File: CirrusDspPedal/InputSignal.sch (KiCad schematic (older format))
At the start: 12 parts, among them J1 MonoJack2Switch, U1 CS5343, U2 74AHC1G126

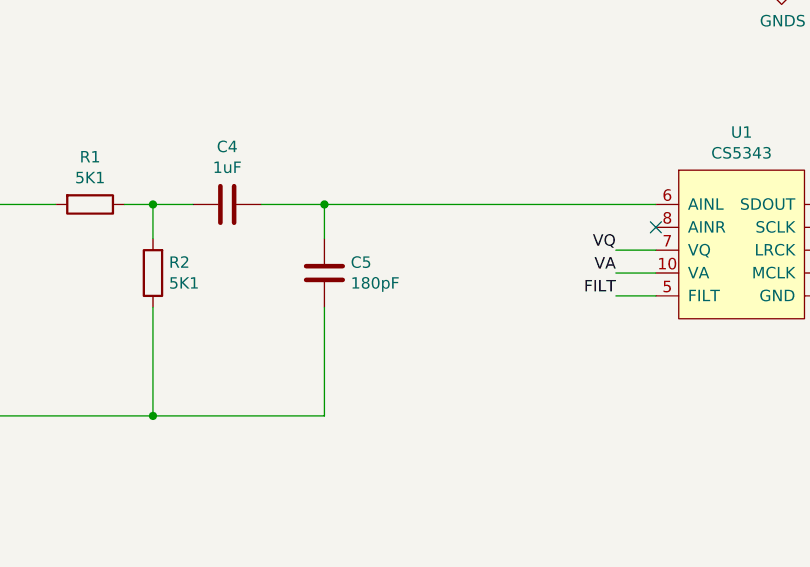
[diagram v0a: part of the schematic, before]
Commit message: Added Footswitches and relay
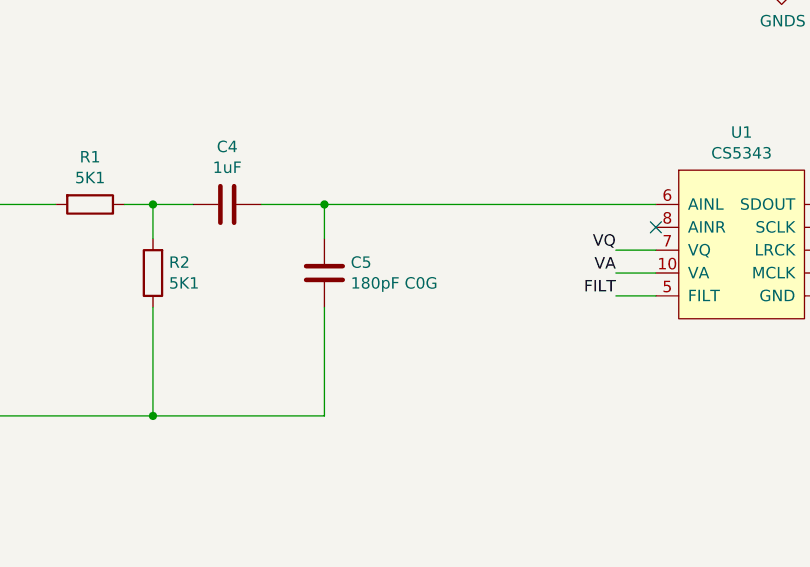
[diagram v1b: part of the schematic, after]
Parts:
- C5: value 180pF -> 180pF C0G
- J1: footprint (none) -> NeutrikNRJ:NRJxHx_NOTAB
- U2: footprint (none) -> Package_TO_SOT_SMD:SOT-23-5_HandSoldering
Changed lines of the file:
@@
 $Descr A4 11693 8268
 encoding utf-8
-Sheet 2 8
+Sheet 2 10
 Title ""
 Date ""
@@
 F 0 "J1" H 2695 4400 50  0000 C CNN
 F 1 "MonoJack2Switch" H 2695 4309 50  0000 C CNN
-F 2 "" H 2600 4075 50  0001 C CNN
+F 2 "NeutrikNRJ:NRJxHx_NOTAB" H 2600 4075 50  0001 C CNN
 F 3 "" H 2600 4075 50  0001 C CNN
 	1    2600 4025
@@
 P 5450 4175
 F 0 "C5" H 5335 4129 50  0000 R CNN
-F 1 "180pF" H 5335 4220 50  0000 R CNN
+F 1 "180pF C0G" H 5335 4220 50  0000 R CNN
 F 2 "Capacitor_SMD:C_0805_2012Metric_Pad1.15x1.40mm_HandSolder" H 5488 4025 50  0001 C CNN
 F 3 "~" H 5450 4175 50  0001 C CNN
@@
 F 0 "U2" H 7650 2775 50  0000 C CNN
 F 1 "74AHC1G126" H 7825 2675 50  0000 C CNN
-F 2 "" H 7400 2500 50  0001 C CNN
+F 2 "Package_TO_SOT_SMD:SOT-23-5_HandSoldering" H 7400 2500 50  0001 C CNN
 F 3 "http://www.ti.com/lit/sg/scyt129e/scyt129e.pdf" H 7400 2500 50  0001 C CNN
 	1    7400 2500

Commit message: updates
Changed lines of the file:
@@
 $Descr A4 11693 8268
 encoding utf-8
-Sheet 2 11
+Sheet 2 10
 Title ""
 Date ""
@@
 S 2350 1375 1525 800
 U 5F85DD92
-F0 "PowerFiltering" 50
+F0 "PwrFilter_CS5343" 50
 F1 "PowerFiltering.sch" 50
 F2 "VDD_OUT" I R 3875 1775 50

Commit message: finished revb layout
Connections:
- net +3V3 renamed +5V
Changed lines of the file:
@@
 Wire Wire Line
 	1775 1775 1775 1575
-$Comp
-L power:+3.3V #PWR0104
-U 1 1 5F864CE6
-P 1775 1575
-F 0 "#PWR0104" H 1775 1425 50  0001 C CNN
-F 1 "+3.3V" H 1790 1748 50  0000 C CNN
-F 2 "" H 1775 1575 50  0001 C CNN
-F 3 "" H 1775 1575 50  0001 C CNN
-	1    1775 1575
-	1    0    0    -1
-$EndComp
 Wire Wire Line
 	3875 1775 4625 1775
@@
 	7400 2300 7400 2175
 $Comp
-L power:+3.3V #PWR0106
-U 1 1 5F88AF93
-P 7400 1675
-F 0 "#PWR0106" H 7400 1525 50  0001 C CNN
-F 1 "+3.3V" H 7415 1848 50  0000 C CNN
-F 2 "" H 7400 1675 50  0001 C CNN
-F 3 "" H 7400 1675 50  0001 C CNN
-	1    7400 1675
-	1    0    0    -1
-$EndComp
-$Comp
 L Device:R R3
 U 1 1 5F88DBC1
@@
 Wire Wire Line
 	6200 6850 6200 7175
-$Comp
-L power:+3.3V #PWR0108
-U 1 1 5F892237
-P 6200 6225
-F 0 "#PWR0108" H 6200 6075 50  0001 C CNN
-F 1 "+3.3V" H 6215 6398 50  0000 C CNN
-F 2 "" H 6200 6225 50  0001 C CNN
-F 3 "" H 6200 6225 50  0001 C CNN
-	1    6200 6225
-	1    0    0    -1
-$EndComp
 Wire Wire Line
 	7450 2450 7450 2175
@@
 	1    0    0    -1
 $EndComp
+$Comp
+L power:+5V #PWR0104
+U 1 1 5FA70BD3
+P 1775 1575
+F 0 "#PWR0104" H 1775 1425 50  0001 C CNN
+F 1 "+5V" H 1790 1748 50  0000 C CNN
+F 2 "" H 1775 1575 50  0001 C CNN
+F 3 "" H 1775 1575 50  0001 C CNN
+	1    1775 1575
+	1    0    0    -1
+$EndComp
+$Comp
+L power:+5V #PWR0106
+U 1 1 5FA72013
+P 7400 1675
+F 0 "#PWR0106" H 7400 1525 50  0001 C CNN
+F 1 "+5V" H 7415 1848 50  0000 C CNN
+F 2 "" H 7400 1675 50  0001 C CNN
+F 3 "" H 7400 1675 50  0001 C CNN
+	1    7400 1675
+	1    0    0    -1
+$EndComp
+$Comp
+L power:+5V #PWR?
+U 1 1 5FA8CC62
+P 6200 6225
+F 0 "#PWR?" H 6200 6075 50  0001 C CNN
+F 1 "+5V" H 6215 6398 50  0000 C CNN
+F 2 "" H 6200 6225 50  0001 C CNN
+F 3 "" H 6200 6225 50  0001 C CNN
+	1    6200 6225
+	1    0    0    -1
+$EndComp

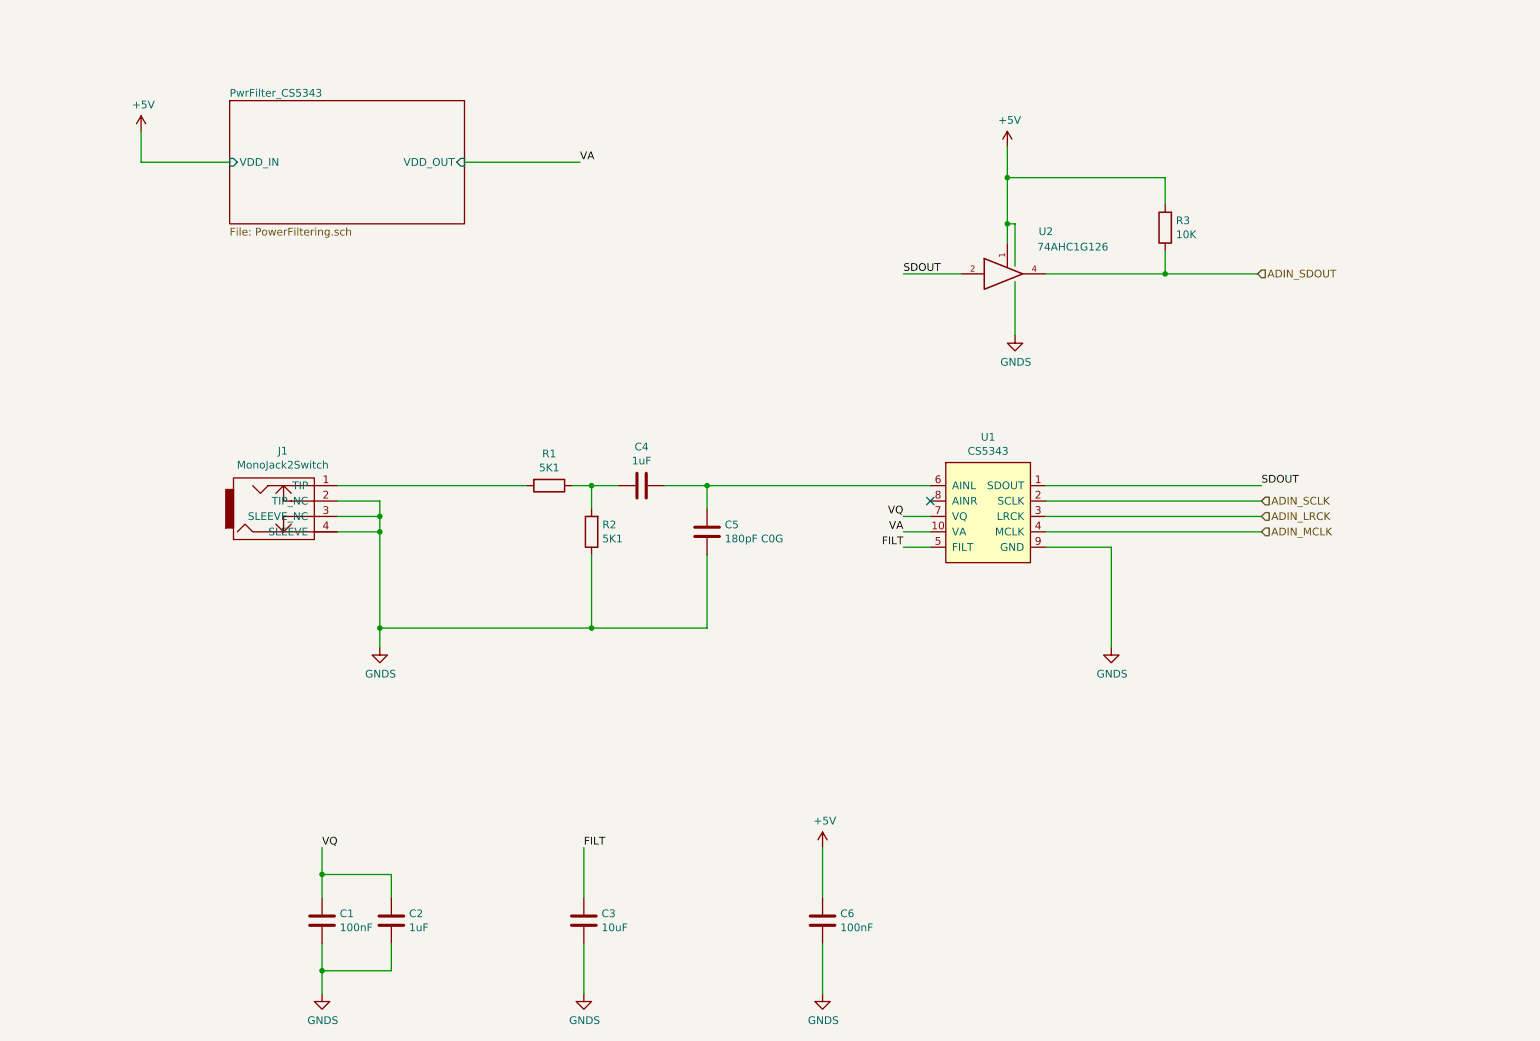
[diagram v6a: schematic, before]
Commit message: updated revb
- Added input amp with charge pump and protection diodes
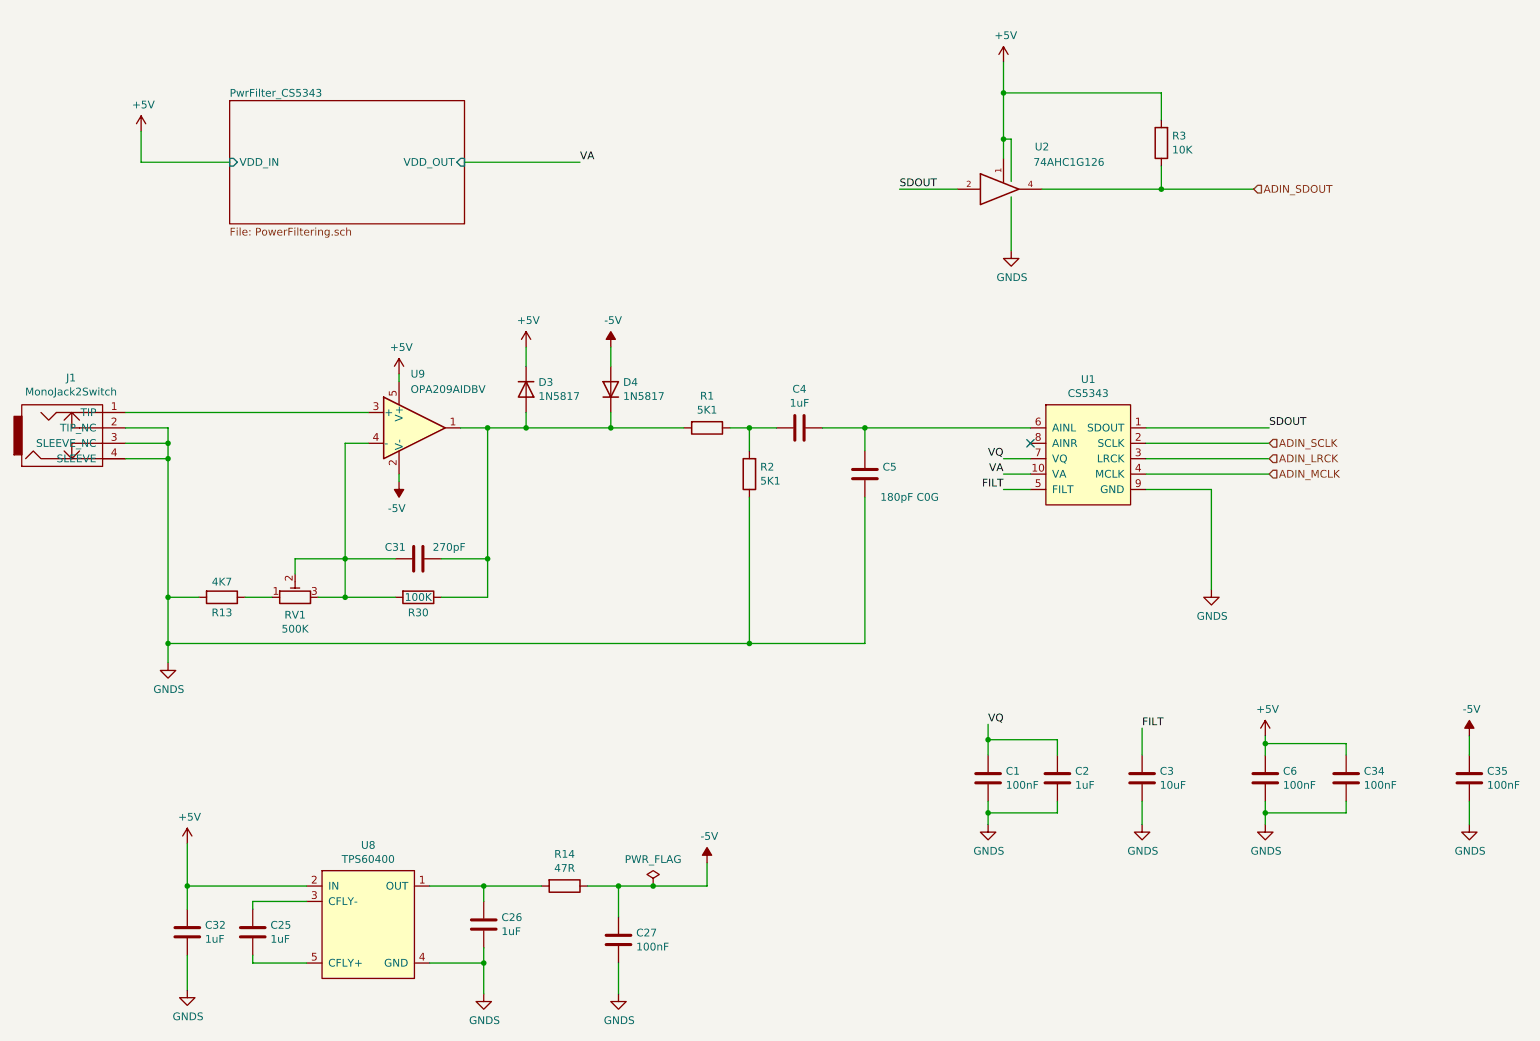
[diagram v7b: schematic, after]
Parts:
- added C25, C26, C32: 1uF, Capacitor_SMD:C_0805_2012Metric_Pad1.18x1.45mm_HandSolder, symbol Device:C
- added C27, C34, C35: 100nF, Capacitor_SMD:C_0805_2012Metric_Pad1.18x1.45mm_HandSolder, symbol Device:C
- added C31: 270pF, Capacitor_SMD:C_0805_2012Metric_Pad1.18x1.45mm_HandSolder, symbol Device:C
- added D3, D4: 1N5817, Diode_SMD:D_SOD-123, symbol Device:D
- added R13: 4K7, Resistor_SMD:R_0805_2012Metric_Pad1.20x1.40mm_HandSolder, symbol Device:R
- added R14: 47R, Resistor_SMD:R_0805_2012Metric_Pad1.20x1.40mm_HandSolder, symbol Device:R
- added R30: 100K, Resistor_SMD:R_0805_2012Metric_Pad1.20x1.40mm_HandSolder, symbol Device:R
- added RV1: 500K, Potentiometer_SMD:Potentiometer_Bourns_3314J_Vertical, symbol Device:R_POT_TRIM
- added U8: TPS60400, Package_TO_SOT_SMD:SOT-23-5_HandSoldering, symbol TPS6040x:TPS60400
- added U9: OPA209AIDBV, Package_TO_SOT_SMD:SOT-23-5, symbol Amplifier_Operational:OPA340NA
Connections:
- net +5V: now also C32.1, C34.1, D3.1 (K), U8.2 (IN), U9.5 (V+)
- net GND: now also C26.2, C27.2, C32.2, C34.2, C35.2, R13.2, U8.4 (GND)
- net at J1.1 (TIP): now also U9.3 (+); no longer R1.2
- new net: C31.1, D3.2 (A), D4.1 (K), R1.2, R30.1, U9.1
- new net: C31.2, R30.2, RV1.2, RV1.3, U9.4 (-)
- new net: C26.1, R14.2, U8.1 (OUT)
- new net: C25.1, U8.3 (CFLY-)
- new net: C25.2, U8.5 (CFLY+)
- new net: R13.1, RV1.1
- new net -5V: C27.1, C35.1, D4.2 (A), R14.1, U9.2 (V-)
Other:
- moved on the sheet: C1, C2, C3, C4, C5, C6, J1, R1, R2, R3, U1, U2

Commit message: updated revb
- Moved THT components to improve UX layout
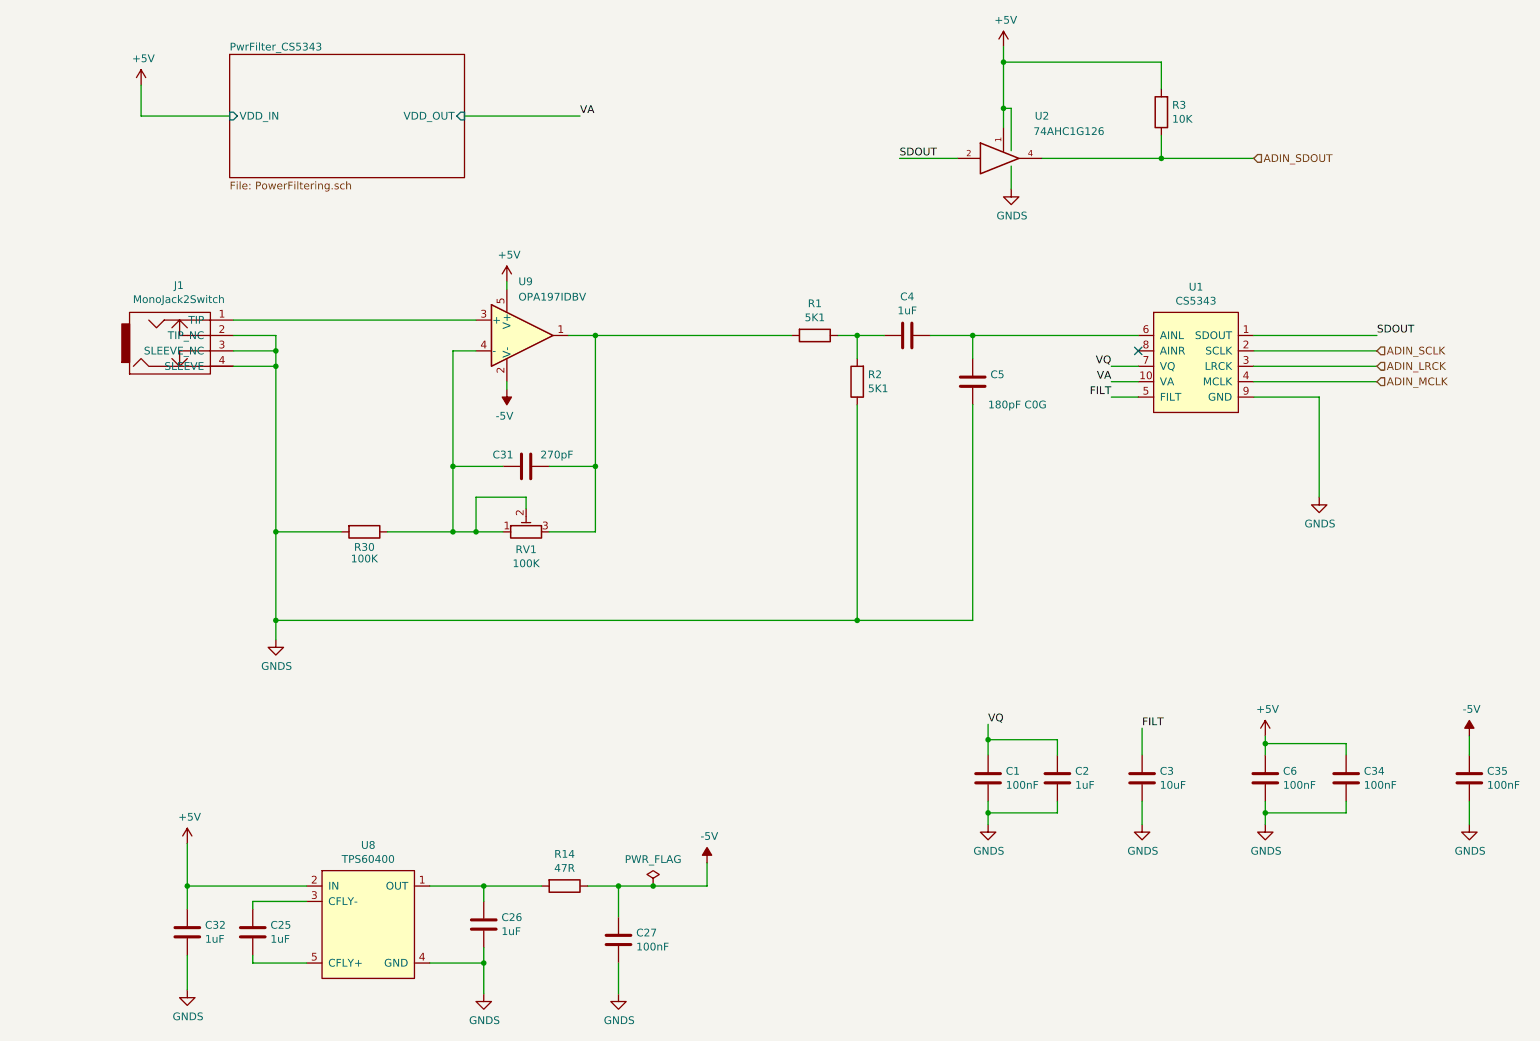
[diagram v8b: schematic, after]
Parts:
- removed D3, D4: 1N5817, Diode_SMD:D_SOD-123, symbol Device:D
- removed R13: 4K7, Resistor_SMD:R_0805_2012Metric_Pad1.20x1.40mm_HandSolder, symbol Device:R
- RV1: value 500K -> 100K
- U9: value OPA209AIDBV -> OPA197IDBV
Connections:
- net GND: now also R30.2
- net at C31.1, R1.2, U9.1: now also RV1.3; no longer R30.1
- net at C31.2, RV1.2, U9.4 (-): now also R30.1, RV1.1; no longer R30.2, RV1.3
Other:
- moved on the sheet: C31, C4, C5, J1, R1, R2, R3, R30, RV1, U1, U2, U9
